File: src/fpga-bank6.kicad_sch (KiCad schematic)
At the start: 1 part

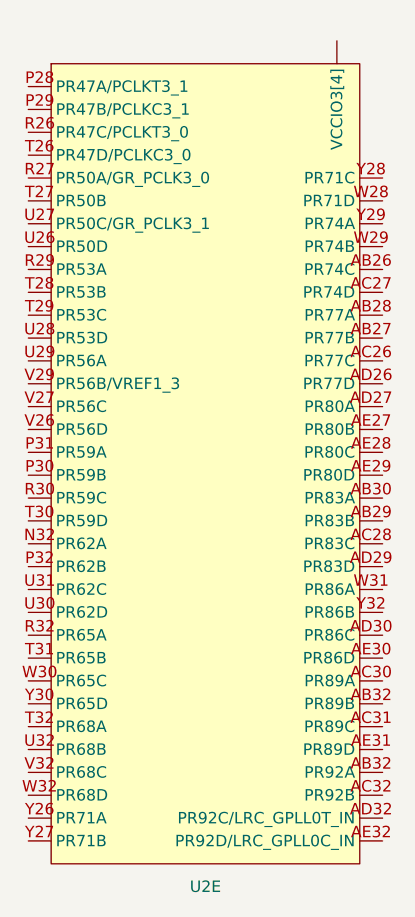
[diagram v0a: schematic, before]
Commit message: Finishes FPGA symbol
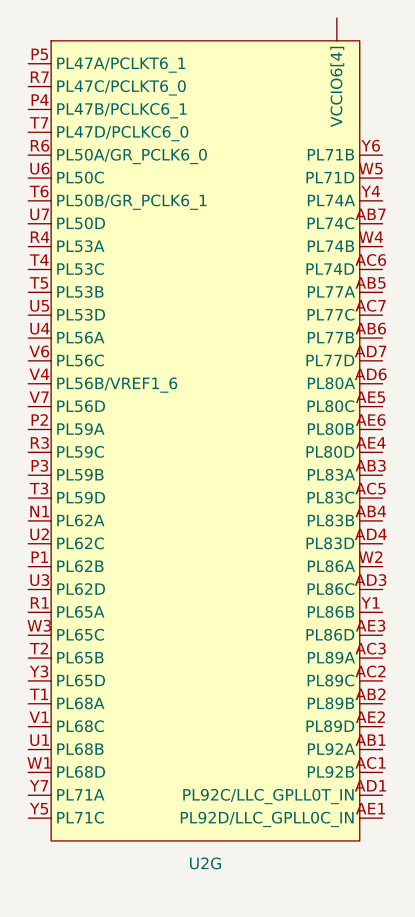
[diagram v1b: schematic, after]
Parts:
- removed U2: ~, symbol ECAP5-BSOM:LFE5U-85F-*BG756*
- added U2: ~, symbol ECAP5-BSOM:LFE5U-85F-*BG756*
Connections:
- new net VCCIO6: U2. (VCCIO6[4]), U2.AA10 (VCCIO6), U2.U10 (VCCIO6), U2.V10 (VCCIO6), U2.W10 (VCCIO6)
